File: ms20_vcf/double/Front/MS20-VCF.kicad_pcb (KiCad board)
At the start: 2 copper layers, 60 x 128 mm, 4 parts

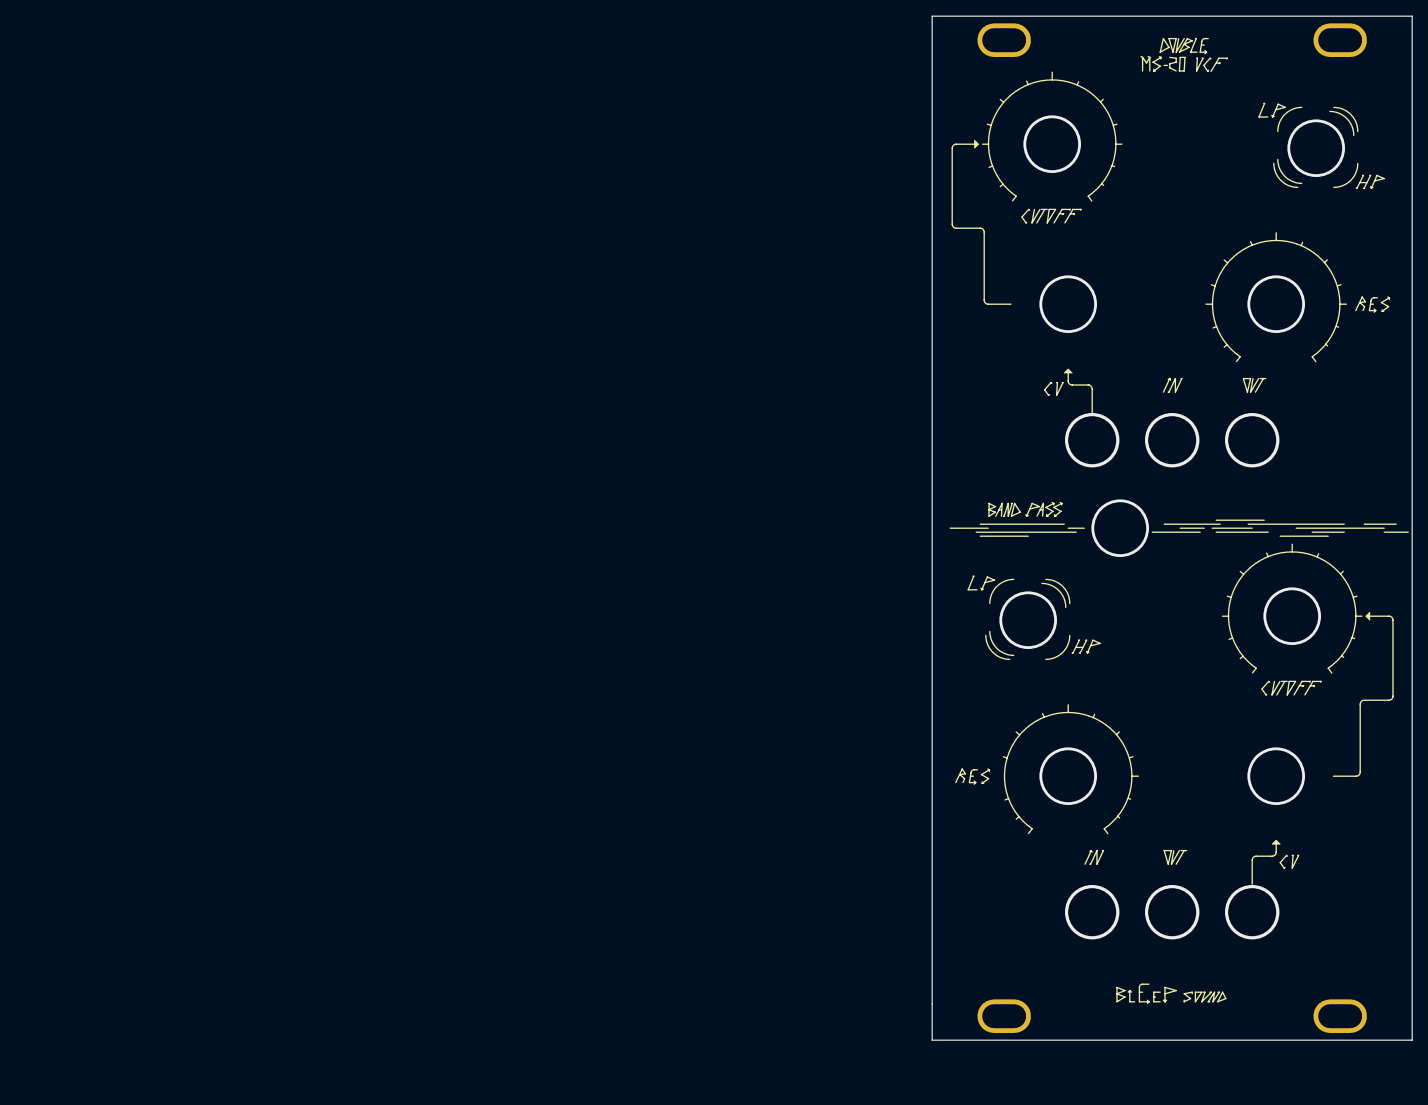
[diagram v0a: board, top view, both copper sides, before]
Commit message: updates front panel designs and gerbers before order
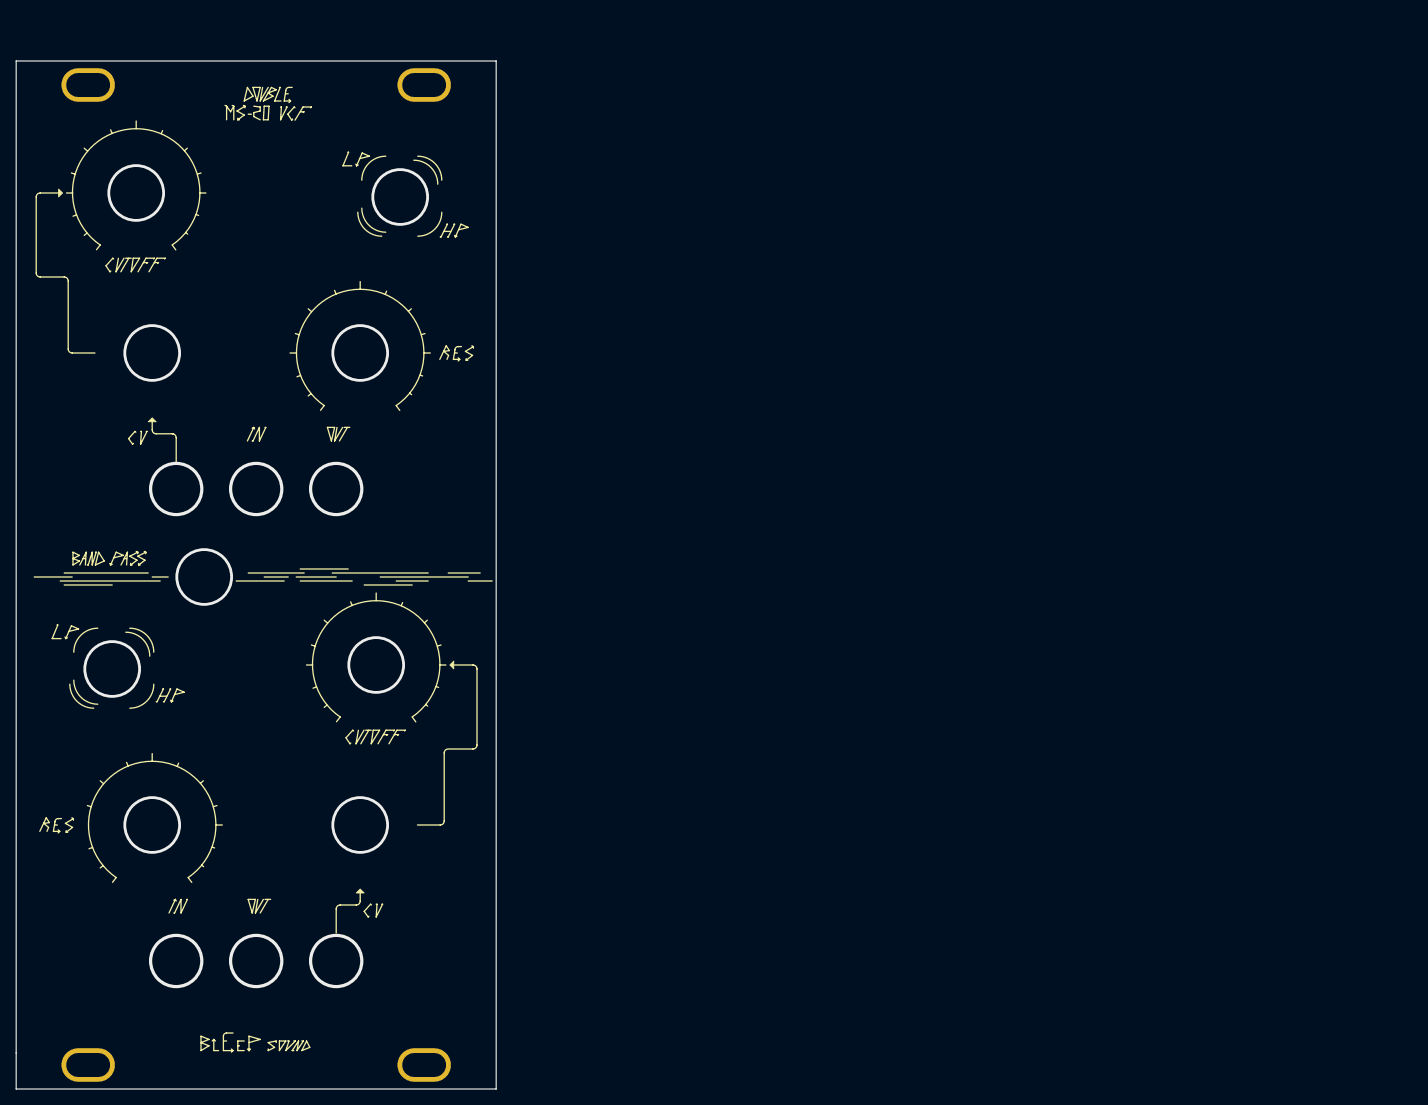
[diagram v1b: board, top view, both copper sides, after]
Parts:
- moved H3 114.7 mm to (113.5, 158.6)
- moved H4 114.7 mm to (71.5, 158.6)
- moved H1 114.6 mm to (71.5, 36.1)
- moved H2 114.6 mm to (113.5, 36.1)
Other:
- board size 60 x 128 mm -> 60 x 128.5 mm
- board text added: "Double MS-20 VCF V1.2 BleepSound 2022"
- board text added: "Front"
